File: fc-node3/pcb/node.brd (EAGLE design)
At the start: 48 x 23 mm, 22 parts, among them IC1 HTU21D, J1 AVR_SPI_PRG_62X3_LOCK, U1 DS18B20

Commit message: routed fc3
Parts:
- moved IC1 12.1 mm to (28.4, 2.29), turned to 90 degrees
- moved C2 4.19 mm to (11.2, 8.13)
- moved R1 4.19 mm to (11.2, 4.06)
- moved R2 4.19 mm to (11.2, 6.10)
- moved R3 4.19 mm to (11.2, 10.2), turned to 180 degrees
- moved U1 3.31 mm to (39.1, 10.9)
- moved U$3 0.92 mm to (22.8, 2.89)
- moved C1 0.76 mm to (16.7, 6.17)
- moved R7 0.76 mm to (35.8, 6.35)
- moved DF 0.76 mm to (4.32, 3.81)
- moved R4 0.51 mm to (35.8, 4.57)
- moved D1 0.25 mm to (7.11, 13.0)
- moved U$1 0.25 mm to (27.9, 9.14)
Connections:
- removed net DIO0: U$1.12, U$4.DIO0
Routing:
- net EN: track 0.00 -> 88.1 mm, vias 0 -> 2
- net VCC: track 91.7 -> 113.9 mm, vias 0 -> 3
- net SCK: track 18.5 -> 40.6 mm, vias 0 -> 2
- net MOSI: track 21.7 -> 36.0 mm
- net MISO: track 19.4 -> 33.2 mm
- net 18B20_DQ: track 34.8 -> 24.8 mm
- net RFM_SS: track 6.90 -> 15.5 mm, vias 0 -> 1
- net N$2: track 5.31 -> 9.25 mm
- net VBATT: track 42.6 -> 39.2 mm
- net DET: track 14.9 -> 13.4 mm
- net RESET: track 22.8 -> 21.5 mm
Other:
- board text added: "+"
- board text added: "AAA 1.5V ONLY"
- board text added: "PV"

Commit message: tidying
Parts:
- moved J1 0.25 mm to (45.7, 4.83)
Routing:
- net VCC: track 113.9 -> 109.9 mm
- net EN: track 88.1 -> 89.6 mm
- net DET: track 13.4 -> 14.4 mm
- net MISO: track 33.2 -> 32.3 mm
- net N$2: track 9.25 -> 8.51 mm
- net SCK: track 40.6 -> 39.9 mm
- net RESET: track 21.5 -> 20.9 mm

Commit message: nicey silky
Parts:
- moved JP1 0.95 mm to (46.0, 11.5)
- renumbered U$2 to U2, U$3 to U3
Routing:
- net VCC: track 109.9 -> 112.8 mm
- net 18B20_DQ: track 24.8 -> 24.3 mm
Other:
- board text added: "18B20"
- board text added: "ANT"
- board text added: "ICSP"
- board text added: "fc-node3"
- board text added: "ukhas.net"
- board text removed: "J SOWMAN"

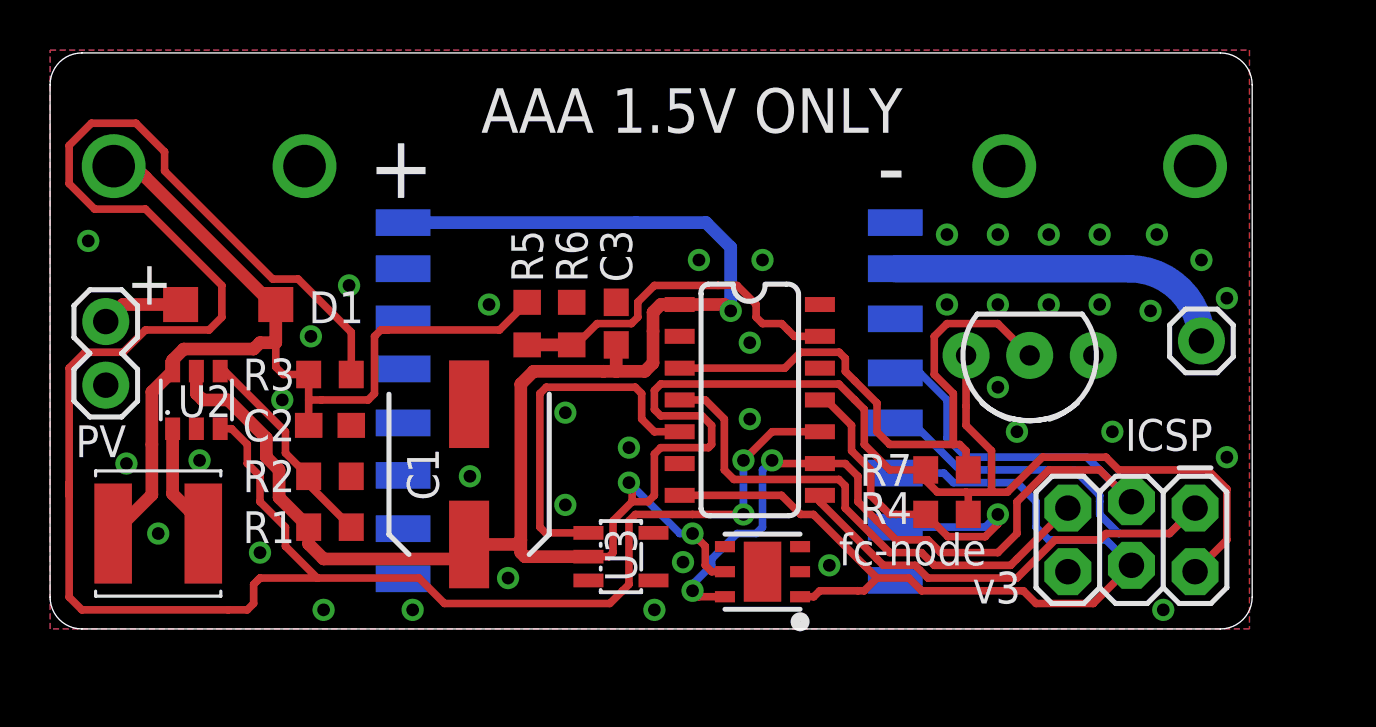
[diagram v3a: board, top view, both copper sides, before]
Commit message: tidying routing for fc3
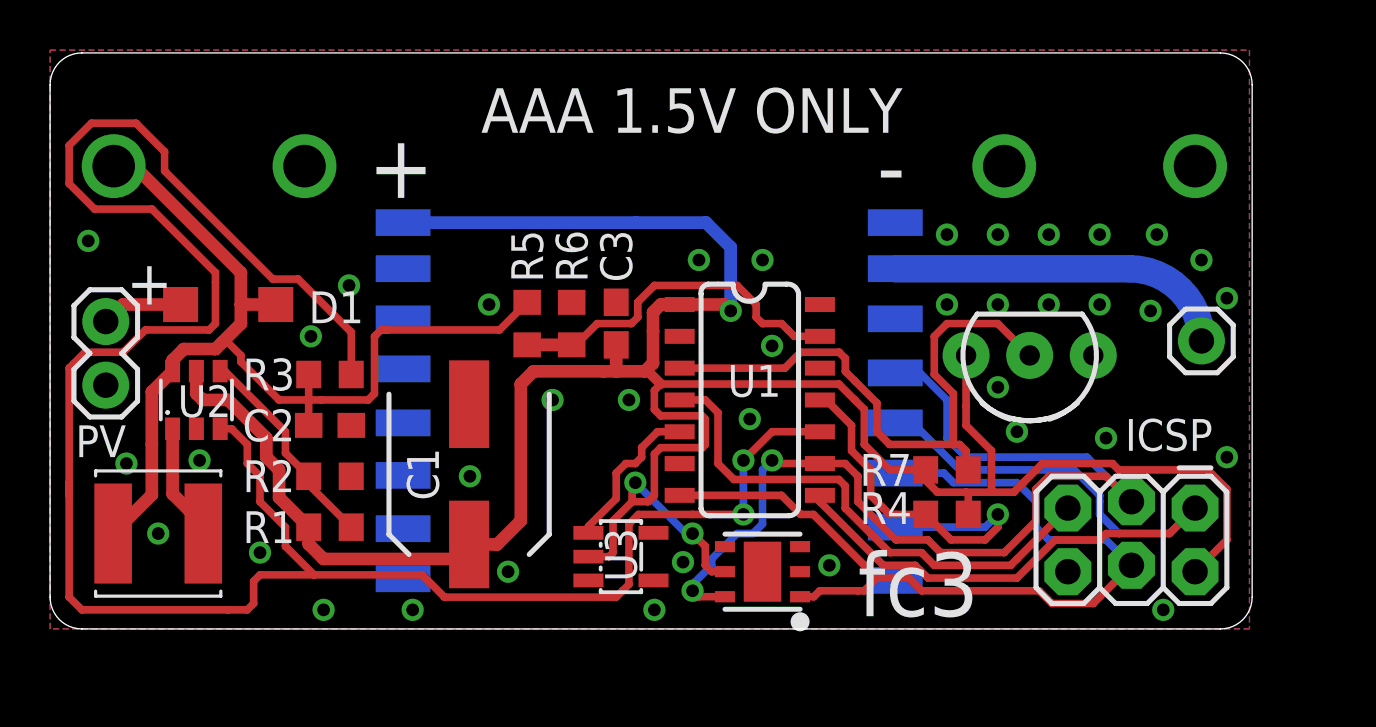
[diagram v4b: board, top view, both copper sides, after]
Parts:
- removed U$1: ATTINY84, SparkFun-DigitalIC:SO14
- added U5: DS18B20, SparkFun-Sensors:TO-92-AMMO
- U1: value DS18B20 -> ATTINY84; device SparkFun-Sensors:TO-92-AMMO -> SparkFun-DigitalIC:SO14
- moved U1 11.3 mm to (27.9, 9.14), turned to 270 degrees
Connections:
- net 18B20_DQ: now also U1.3, U5.2; no longer U$1.3, U1.2
- net DET: now also U1.5; no longer U$1.5
- net EN: now also U1.10; no longer U$1.10
- net GND: now also U1.14, U5.1; no longer U$1.14, U1.1
- net MISO: now also U1.8; no longer U$1.8
- net MOSI: now also U1.7; no longer U$1.7
- net N$6: now also U1.6; no longer U$1.6
- net RESET: now also U1.4; no longer U$1.4
- net RFM_SS: now also U1.11; no longer U$1.11
- net SCK: now also U1.9; no longer U$1.9
- net VCC: now also U1.1, U5.3; no longer U$1.1, U1.3
- net VSENSE: now also U1.13; no longer U$1.13
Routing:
- net DET: track 14.4 -> 6.29 mm
- net VCC: track 112.8 -> 109.1 mm
- net VBATT: track 39.2 -> 40.4 mm
- net EN: track 89.6 -> 89.0 mm
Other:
- board text added: "fc3"
- board text removed: "fc-node"
- board text removed: "v3"
